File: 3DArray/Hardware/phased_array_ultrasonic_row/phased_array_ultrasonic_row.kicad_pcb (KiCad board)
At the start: 2 copper layers, 224.3 x 23.5 mm, 34 parts, among them J1 Conn_02x09_Counter_Clockwise, J2 Conn_02x09_Counter_Clockwise, U1 SN74HC157, U2 SN74HC157, U3 TC4427AVPA, U4 CD4517BE, U5 TC4427AVPA, U6 CD4517BE, U7 TC4427AVPA, U8 CD4517BE

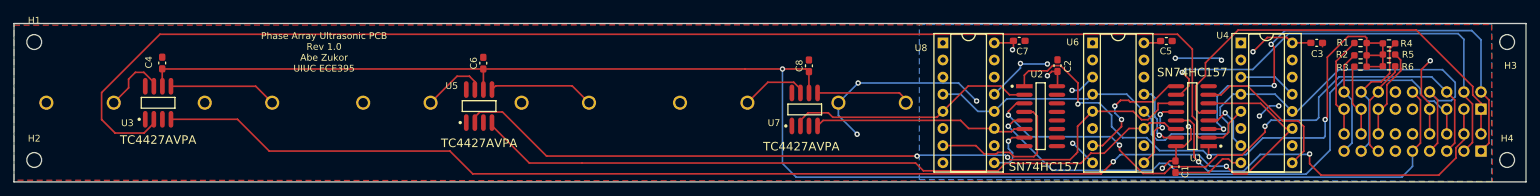
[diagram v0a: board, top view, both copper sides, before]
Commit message: Fixed pcb mux inpits swapped for C6, C6.
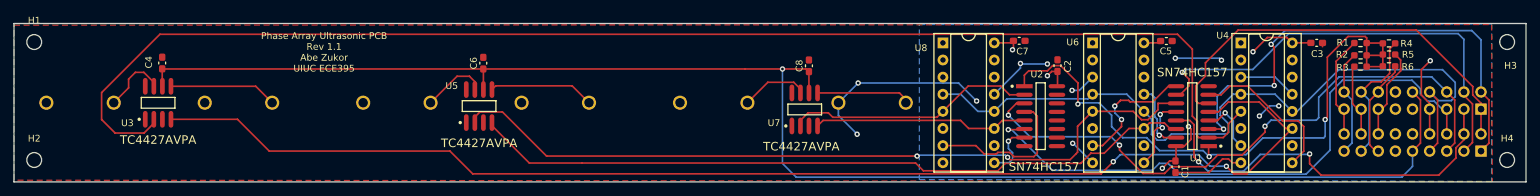
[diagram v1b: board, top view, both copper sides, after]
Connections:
- U1 pad 5: /C2 -> /Speakers12/SigB
- U1 pad 6: /Speakers12/SigB -> /C2
- U2 pad 5: /C6 -> /Speakers56/SigB
- U2 pad 6: /Speakers56/SigB -> /C6
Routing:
- net /C2: track 63.3 -> 61.9 mm
- net /Speakers12/SigB: track 188.8 -> 189.7 mm
- net /Speakers56/SigB: track 31.9 -> 32.7 mm
- net /C6: track 88.3 -> 87.7 mm
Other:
- board text added: "Phase Array Ultrasonic PCB Rev 1.1 Abe Zukor UIUC ECE395"
- board text removed: "Phase Array Ultrasonic PCB Rev 1.0 Abe Zukor UIUC ECE395"
